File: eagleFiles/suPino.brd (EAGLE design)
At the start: 72.1 x 63.5 mm, 25 parts

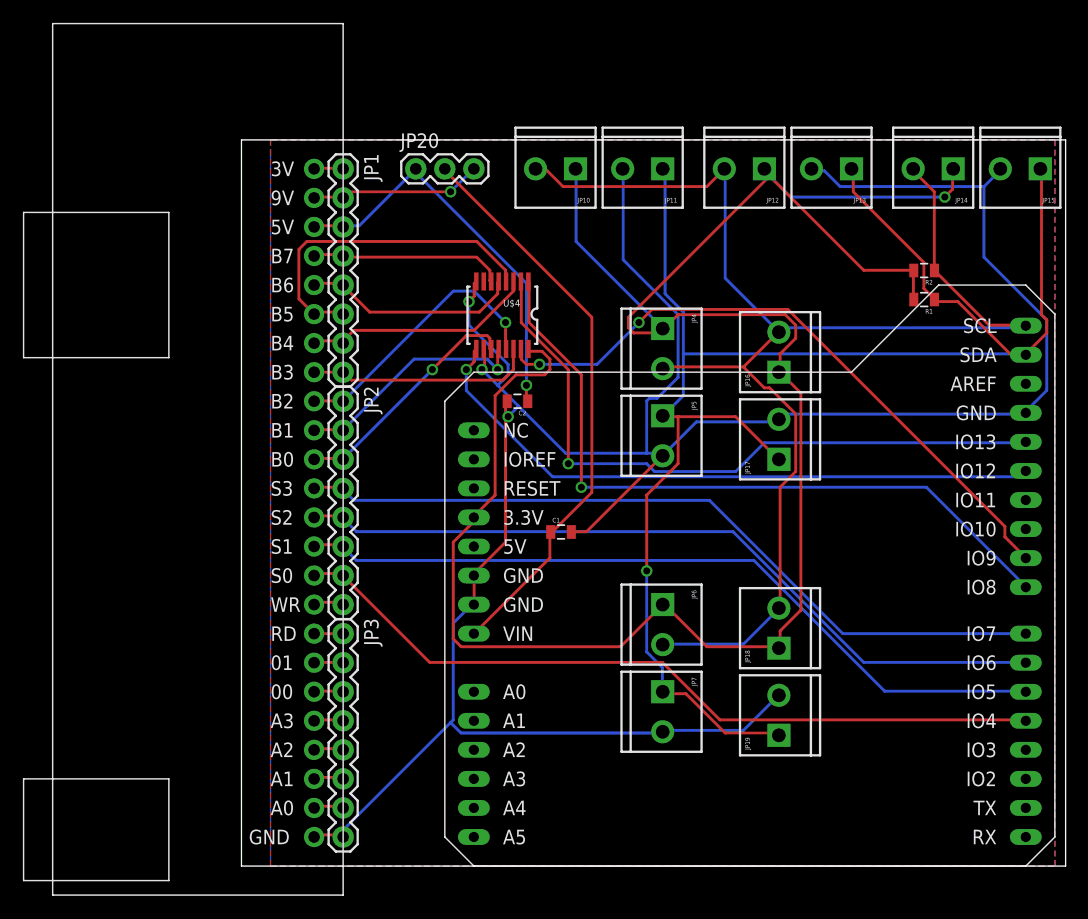
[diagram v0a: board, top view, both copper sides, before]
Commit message: Fixed the routing and added silkscreen
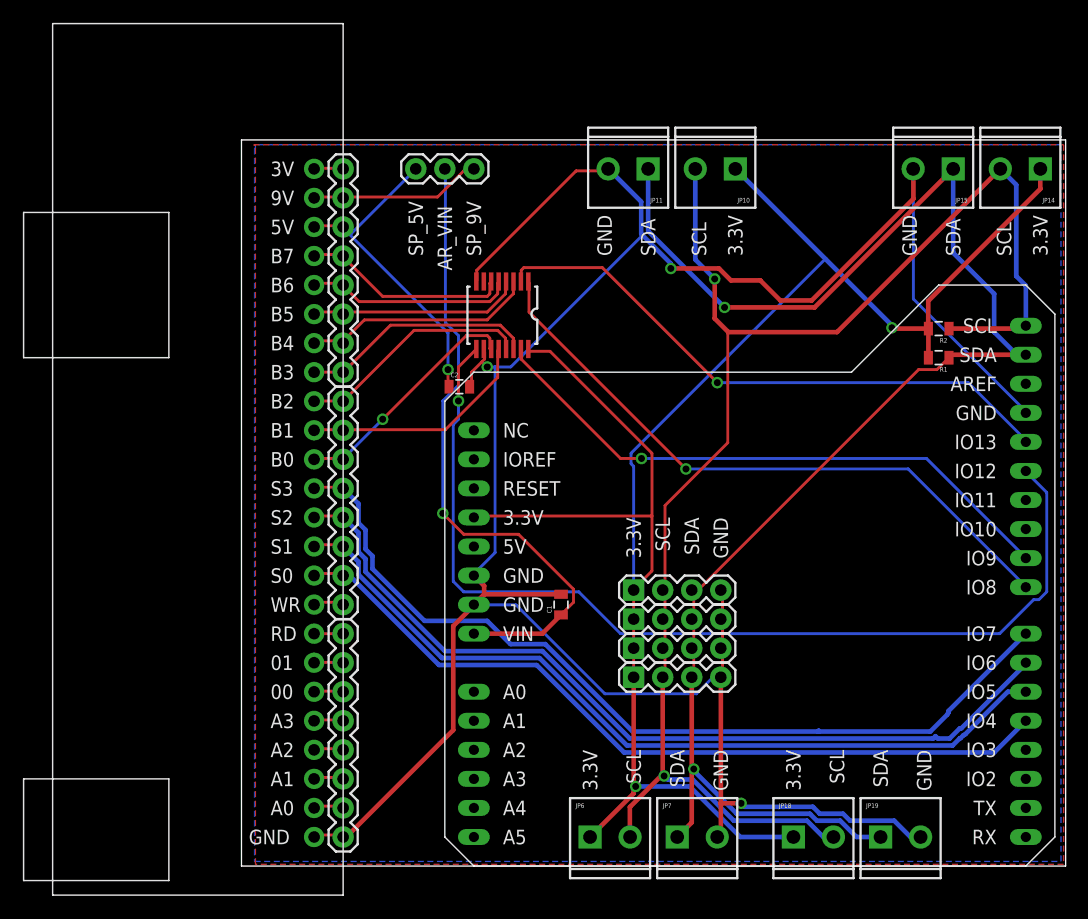
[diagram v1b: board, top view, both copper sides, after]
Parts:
- removed JP12, JP13, JP16, JP17: M023.5MM, SparkFun-Connectors:SCREWTERMINAL-3.5MM-2
- added JP8, JP9: (no value), SparkFun-Connectors:1X04
- JP4, JP5: value M023.5MM -> (none); device SparkFun-Connectors:SCREWTERMINAL-3.5MM-2 -> SparkFun-Connectors:1X04
- moved JP4 28.1 mm to (34.3, 21.6), turned to 0 degrees
- moved JP5 23.0 mm to (34.3, 19.1), turned to 0 degrees
- moved JP6 21.3 mm to (30.5, 5.08), turned to 0 degrees
- moved JP18 16.6 mm to (48.3, 5.08), turned to 0 degrees
- moved JP10 14.0 mm to (43.2, 63.5)
- moved JP7 12.8 mm to (38.1, 5.08), turned to 0 degrees
- moved JP19 12.6 mm to (55.9, 5.08), turned to 0 degrees
- moved JP14 7.62 mm to (69.8, 63.5)
- moved JP15 7.62 mm to (62.2, 63.5)
- moved C1 6.35 mm to (27.9, 25.4), turned to 90 degrees
- moved C2 5.24 mm to (19.1, 44.5), turned to 0 degrees
- moved R1 5.24 mm to (61.0, 47.0)
- moved R2 5.24 mm to (61.0, 49.5)
- moved JP11 1.27 mm to (35.6, 63.5)
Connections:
- net AR_3.3V: now also JP5.1, JP8.1, JP9.1; no longer JP12.1, JP16.1
- net DGND: now also JP4.4, JP5.4, JP8.4, JP9.4; no longer JP13.2, JP17.2, JP5.2
- net I2C_SCL: now also JP5.2, JP8.2, JP9.2; no longer JP12.2, JP16.2
- net I2C_SDA: now also JP4.3, JP5.3, JP8.3, JP9.3; no longer JP13.1, JP17.1, JP5.1
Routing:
- net SPI_MISO: track 56.3 -> 87.8 mm
- net AR_3.3V: track 185.3 -> 161.4 mm, vias 1 -> 2
- net SP_B5: track 29.3 -> 18.8 mm
- net SP_S3: track 67.6 -> 77.5 mm
- net I2C_SCL: track 122.5 -> 132.3 mm, vias 0 -> 2
- net SPI_SCK: track 59.0 -> 51.6 mm
- net SP_S2: track 67.7 -> 75.0 mm
- net SHIFT_LOAD: track 62.4 -> 56.1 mm
- net AR_VIN: track 50.3 -> 56.3 mm, vias 0 -> 1
- net SP_5V: track 35.4 -> 29.4 mm
- net I2C_SDA: track 144.0 -> 138.7 mm, vias 1 -> 2
- net SHIFT_LATCH: track 56.7 -> 52.2 mm, vias 2 -> 1
- net SP_S1: track 67.7 -> 72.2 mm
- net SP_B2: track 24.2 -> 20.6 mm, vias 1 -> 0
- net DGND: track 224.1 -> 227.4 mm
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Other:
- board text added: "3.3V"
- board text added: "AR_VIN"
- board text added: "GND"
- board text added: "SCL"
- board text added: "SDA"
- board text added: "SP_5V"
- board text added: "SP_9V"
